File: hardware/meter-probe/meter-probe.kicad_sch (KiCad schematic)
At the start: 49 parts, among them J1 Cable, SW1 Sensor Button, U1 TSL2585, U2 USBLC6-2SC6, U3 MIC5365-1.8YC5, U4 FT260Q, U5 CAT24C08

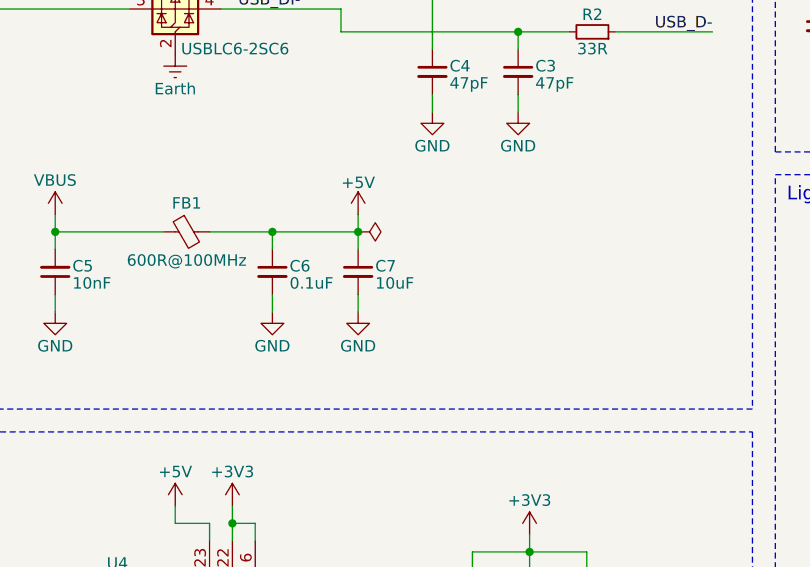
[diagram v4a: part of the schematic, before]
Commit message: Change bulk input capacitor to 4.7uF and nudge some traces
Safer to just stick with the lower value for now, and reevaluate later
if necessary, due to USB inrush rules.

Ref #65
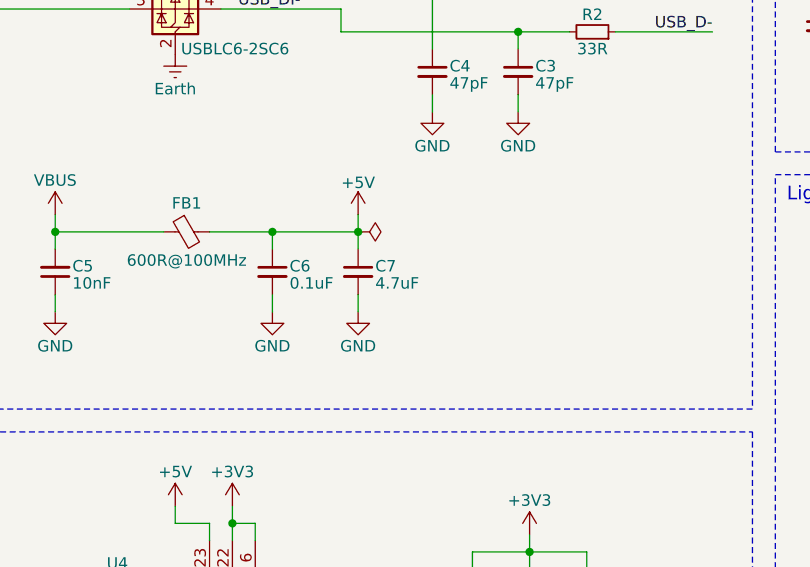
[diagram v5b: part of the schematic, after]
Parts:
- C7: value 10uF -> 4.7uF; footprint Capacitor_SMD:C_0805_2012Metric -> Capacitor_SMD:C_0603_1608Metric; Manufacturer PN CL21A106KAYNNNE -> CL10A475KA8NQNC; Supplier Digi-Key -> LCSC; Supplier PN 1276-2891-1-ND -> C69335
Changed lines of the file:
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@@
 	)
 	(symbol
+		(lib_id "Device:C_Small")
+		(at 83.185 59.055 0)
+		(unit 1)
+		(exclude_from_sim no)
+		(in_bom yes)
+		(on_board yes)
+		(dnp no)
+		(property "Reference" "C7"
+			(at 85.09 58.42 0)
+			(effects
+				(font
+					(size 1.27 1.27)
+				)
+				(justify left)
+			)
+		)
+		(property "Value" "4.7uF"
+			(at 85.09 60.325 0)
+			(effects
+				(font
+					(size 1.27 1.27)
+				)
+				(justify left)
+			)
+		)
+		(property "Footprint" "Capacitor_SMD:C_0603_1608Metric"
+			(at 83.185 59.055 0)
+			(effects
+				(font
+					(size 1.27 1.27)
+				)
+				(hide yes)
+			)
+		)
+		(property "Datasheet" "https://media.digikey.com/pdf/Data%20Sheets/Samsung%20PDFs/CL10A475KA8NQNC_Spec.pdf"
+			(at 83.185 59.055 0)
+			(effects
+				(font
+					(size 1.27 1.27)
+				)
+				(hide yes)
+			)
+		)
+		(property "Description" "CAP CER 4.7UF 25V X5R 0603"
+			(at 83.185 59.055 0)
+			(effects
+				(font
+					(size 1.27 1.27)
+				)
+				(hide yes)
+			)
+		)
+		(property "Manufacturer" "Samsung Electro-Mechanics"
+			(at 83.185 59.055 0)
+			(effects
+				(font
+					(size 1.27 1.27)
+				)
+				(hide yes)
+			)
+		)
+		(property "Manufacturer PN" "CL10A475KA8NQNC"
+			(at 83.185 59.055 0)
+			(effects
+				(font
+					(size 1.27 1.27)
+				)
+				(hide yes)
+			)
+		)
+		(property "Supplier" "LCSC"
+			(at 83.185 59.055 0)
+			(effects
+				(font
+					(size 1.27 1.27)
+				)
+				(hide yes)
+			)
+		)
+		(property "Supplier PN" "C69335"
+			(at 83.185 59.055 0)
+			(effects
+				(font
+					(size 1.27 1.27)
+				)
+				(hide yes)
+			)
+		)
+		(pin "1"
+		)
+		(pin "2"
+		)
+		(instances
+			(project "meter-probe"
+				(path "/1f1005f7-3f58-4453-9bfa-bdc1c0b6f7ed"
+					(reference "C7")
+					(unit 1)
+				)
+			)
+		)
+	)
+	(symbol
 		(lib_id "Device:R_Small")
 		(at 95.885 94.615 0)
@@
 					(unit 1)
 				)
-			)
-			(project "main-board"
-				(path "/31a301d9-d769-4a35-943a-fe3e3609e773/00000000-0000-0000-0000-00005fa19aff"
-					(reference "C?")
-					(unit 1)
-				)
-			)
-		)
-	)
-	(symbol
-		(lib_id "Device:C_Small")
-		(at 83.185 59.055 0)
-		(unit 1)
-		(exclude_from_sim no)
-		(in_bom yes)
-		(on_board yes)
-		(dnp no)
-		(property "Reference" "C7"
-			(at 85.09 58.42 0)
-			(effects
-				(font
-					(size 1.27 1.27)
-				)
-				(justify left)
-			)
-		)
-		(property "Value" "10uF"
-			(at 85.09 60.325 0)
-			(effects
-				(font
-					(size 1.27 1.27)
-				)
-				(justify left)
-			)
-		)
-		(property "Footprint" "Capacitor_SMD:C_0805_2012Metric"
-			(at 84.1502 62.865 0)
-			(effects
-				(font
-					(size 1.27 1.27)
-				)
-				(hide yes)
-			)
-		)
-		(property "Datasheet" "https://mm.digikey.com/Volume0/opasdata/d220001/medias/docus/5545/CL21A106KAYNNNE%20Spec.pdf"
-			(at 83.185 59.055 0)
-			(effects
-				(font
-					(size 1.27 1.27)
-				)
-				(hide yes)
-			)
-		)
-		(property "Description" "CAP CER 10UF 25V X5R 0805"
-			(at 83.185 59.055 0)
-			(effects
-				(font
-					(size 1.27 1.27)
-				)
-				(hide yes)
-			)
-		)
-		(property "Manufacturer" "Samsung Electro-Mechanics"
-			(at 83.185 59.055 0)
-			(effects
-				(font
-					(size 1.27 1.27)
-				)
-				(hide yes)
-			)
-		)
-		(property "Manufacturer PN" "CL21A106KAYNNNE"
-			(at 83.185 59.055 0)
-			(effects
-				(font
-					(size 1.27 1.27)
-				)
-				(hide yes)
-			)
-		)
-		(property "Supplier" "Digi-Key"
-			(at 83.185 59.055 0)
-			(effects
-				(font
-					(size 1.27 1.27)
-				)
-				(hide yes)
-			)
-		)
-		(property "Supplier PN" "1276-2891-1-ND"
-			(at 83.185 59.055 0)
-			(effects
-				(font
-					(size 1.27 1.27)
-				)
-				(hide yes)
-			)
-		)
-		(pin "1"
-		)
-		(pin "2"
-		)
-		(instances
-			(project "meter-probe"
-				(path "/1f1005f7-3f58-4453-9bfa-bdc1c0b6f7ed"
-					(reference "C7")
-					(unit 1)
-				)
